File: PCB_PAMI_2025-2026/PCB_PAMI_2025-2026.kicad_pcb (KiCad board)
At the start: 2 copper layers, 125 x 84 mm, 63 parts, among them J1 BAU, J10 MOTOR 4, J11 COMM_inter_mcu, J12 USB_C_Receptacle_USB2.0_16P, J13 BOOST_OUT, J2 BAT+, J3 VIN_Connector, J4 BAT-, J6 BOOST_IN, J7 MOTOR 3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

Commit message: corrections pins drivers trop proches
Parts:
- moved J9 1.62 mm to (131.3, 45.7)
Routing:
- net /3V3: track 152.4 -> 160.7 mm
- net /ENC2_2: track 66.5 -> 68.9 mm
- net /AOUT1: track 18.1 -> 19.8 mm
- net GND: track 108.5 -> 107.6 mm, vias 30 -> 28
- net /ENC1_1: track 54.8 -> 54.1 mm
- net /AOUT2: track 4.97 -> 5.64 mm
- net /ENC1_2: track 60.3 -> 59.6 mm
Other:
- outline, holes or cut-outs redrawn
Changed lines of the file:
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@@
 	(footprint "Connector_PinHeader_2.54mm:PinHeader_1x06_P2.54mm_Vertical"
 		(layer "F.Cu")
-		(at 131.34 44.1 90)
+		(at 131.34 45.72 90)
 		(descr "Through hole straight pin header, 1x06, 2.54mm pitch, single row")
 		(tags "Through hole pin header THT 1x06 2.54mm single row")
@@
 	)
 	(gr_rect
-		(start 94 35.9)
-		(end 98 43.9)
+		(start 87.44 36.64)
+		(end 97.98 40.64)
 		(stroke
 			(width 0.2)
@@
 	)
 	(gr_rect
-		(start 94 68)
-		(end 98 76)
+		(start 87.44 69.66)
+		(end 97.98 73.66)
 		(stroke
 			(width 0.2)
@@
 	)
 	(segment
+		(start 133.799 54.795423)
+		(end 137.494423 51.1)
+		(width 1.5)
+		(layer "F.Cu")
+		(net 2)
+	)
+	(segment
 		(start 132.3 55.5)
 		(end 132.2 55.4)
@@
 	)
 	(segment
+		(start 137.494423 51.1)
+		(end 138 51.1)
+		(width 1.5)
+		(layer "F.Cu")
+		(net 2)
+	)
+	(segment
 		(start 161.1 25.75)
 		(end 161.1 24.93)
@@
 	)
 	(segment
-		(start 137.16 60.96)
-		(end 137.16 58.24)
-		(width 1.5)
-		(layer "F.Cu")
-		(net 2)
-	)
-	(segment
 		(start 55.43 93.75)
 		(end 57.15 93.75)
@@
 	)
 	(segment
-		(start 133.799 54.795423)
-		(end 140.194423 48.4)
-		(width 1.5)
-		(layer "F.Cu")
-		(net 2)
-	)
-	(segment
 		(start 142.24 88.46)
 		(end 142.3 88.4)
@@
 	)
 	(segment
-		(start 140.194423 48.4)
-		(end 141.5 48.4)
-		(width 1.5)
-		(layer "F.Cu")
-		(net 2)
-	)
-	(segment
 		(start 161.524264 26.9)
 		(end 161.6 26.975736)
@@
 		(net 2)
 	)
-	(segment
-		(start 137.16 58.24)
-		(end 137.2 58.2)
-		(width 1.5)
-		(layer "F.Cu")
-		(net 2)
-	)
 	(via
 		(at 73.5 67.7)
@@
 	)
 	(via
-		(at 137.2 58.2)
-		(size 0.6)
-		(drill 0.3)
-		(layers "F.Cu" "B.Cu")
-		(net 2)
-	)
-	(via
 		(at 115 44.1)
 		(size 0.6)
@@
 	)
 	(via
-		(at 141.5 48.4)
-		(size 0.6)
-		(drill 0.3)
-		(layers "F.Cu" "B.Cu")
-		(net 2)
-	)
-	(via
 		(at 115 68.2)
 		(size 0.6)
@@
 	)
 	(segment
+		(start 138 51.1)
+		(end 144.2 51.1)
+		(width 1.5)
+		(layer "B.Cu")
+		(net 2)
+	)
+	(segment
 		(start 141.5 39.9)
 		(end 141.5 37.1)
@@
 	)
 	(segment
+		(start 144.2 51.1)
+		(end 144.4 51.3)
+		(width 1.5)
+		(layer "B.Cu")
+		(net 2)
+	)
+	(segment
 		(start 148.485 32.8)
 		(end 148.525 32.76)
@@
 	)
 	(segment
-		(start 169.825 28.725)
-		(end 169.9 28.8)
+		(start 133.88 45.72)
+		(end 133.88 39.9)
 		(width 1)
 		(layer "F.Cu")
@@
 	)
 	(segment
-		(start 133.88 44.1)
-		(end 133.88 39.9)
+		(start 169.825 28.725)
+		(end 169.9 28.8)
 		(width 1)
 		(layer "F.Cu")
@@
 	)
 	(segment
+		(start 133.88 40.462)
+		(end 133.88 39.9)
+		(width 1)
+		(layer "B.Cu")
+		(net 7)
+	)
+	(segment
 		(start 126.3 41.838)
 		(end 139.338 28.8)
@@
 	)
 	(segment
-		(start 126.3 45.651)
-		(end 126.3 41.838)
+		(start 133.88 44.517919)
+		(end 133.88 45.72)
 		(width 1)
 		(layer "B.Cu")
@@
 	)
 	(segment
-		(start 132.649 45.651)
-		(end 133.88 44.42)
+		(start 133.083081 43.721)
+		(end 133.88 44.517919)
+		(width 1)
+		(layer "B.Cu")
+		(net 7)
+	)
+	(segment
+		(start 126.3 45.651)
+		(end 126.3 41.838)
 		(width 1)
 		(layer "B.Cu")
@@
 	)
 	(segment
+		(start 130.621 43.721)
+		(end 133.88 40.462)
+		(width 1)
+		(layer "B.Cu")
+		(net 7)
+	)
+	(segment
 		(start 94.8 45.5)
 		(end 94.951 45.651)
@@
 	)
 	(segment
+		(start 130.621 43.721)
+		(end 133.083081 43.721)
+		(width 1)
+		(layer "B.Cu")
+		(net 7)
+	)
+	(segment
 		(start 126.3 45.651)
-		(end 132.649 45.651)
+		(end 128.691 45.651)
 		(width 1)
 		(layer "B.Cu")
@@
 	)
 	(segment
-		(start 133.88 44.42)
-		(end 133.88 44.1)
+		(start 128.691 45.651)
+		(end 130.621 43.721)
 		(width 1)
 		(layer "B.Cu")
@@
 	)
 	(segment
-		(start 138.768884 39.9)
-		(end 135.056 43.612884)
+		(start 138.96 39.9)
+		(end 138.768884 39.9)
 		(width 0.25)
 		(layer "B.Cu")
@@
 	)
 	(segment
-		(start 135.056 44.587116)
-		(end 133.166116 46.477)
+		(start 138.96 39.9)
+		(end 135.1 43.76)
 		(width 0.25)
 		(layer "B.Cu")
@@
 	)
 	(segment
-		(start 138.96 39.9)
-		(end 138.768884 39.9)
+		(start 133.3 48.045)
+		(end 96.17686 48.045)
 		(width 0.25)
 		(layer "B.Cu")
@@
 	)
 	(segment
-		(start 94.60886 46.477)
-		(end 94.37586 46.244)
+		(start 77.396 46.244)
+		(end 76.27 47.37)
 		(width 0.25)
 		(layer "B.Cu")
@@
 	)
 	(segment
-		(start 133.166116 46.477)
-		(end 94.60886 46.477)
+		(start 94.37586 46.244)
+		(end 77.396 46.244)
 		(width 0.25)
 		(layer "B.Cu")
@@
 	)
 	(segment
-		(start 94.37586 46.244)
-		(end 77.396 46.244)
+		(start 96.17686 48.045)
+		(end 94.37586 46.244)
 		(width 0.25)
 		(layer "B.Cu")
@@
 	)
 	(segment
-		(start 77.396 46.244)
-		(end 76.27 47.37)
+		(start 135.1 43.76)
+		(end 135.1 46.245)
 		(width 0.25)
 		(layer "B.Cu")
@@
 	)
 	(segment
-		(start 135.056 43.612884)
-		(end 135.056 44.587116)
+		(start 135.1 46.245)
+		(end 133.3 48.045)
 		(width 0.25)
 		(layer "B.Cu")
@@
 	)
 	(segment
-		(start 134.113 48.947)
-		(end 82.927 48.947)
+		(start 82.927 48.947)
+		(end 135.733 48.947)
 		(width 0.25)
 		(layer "B.Cu")
@@
 	)
 	(segment
-		(start 82.927 48.947)
-		(end 81.35 47.37)
+		(start 81.35 47.37)
+		(end 82.927 48.947)
 		(width 0.25)
 		(layer "B.Cu")
@@
 	)
 	(segment
-		(start 138.96 44.1)
-		(end 134.113 48.947)
+		(start 135.733 48.947)
+		(end 138.96 45.72)
 		(width 0.25)
 		(layer "B.Cu")
@@
 	(segment
 		(start 148.525 45.46)
-		(end 148.084 45.901)
+		(end 147.84 45.46)
+		(width 1.5)
+		(layer "F.Cu")
+		(net 27)
+	)
+	(segment
+		(start 145 48.3)
+		(end 133.3 48.3)
 		(width 1.5)
 		(layer "F.Cu")
@@
 	)
 	(segment
-		(start 133.134001 45.901)
-		(end 131.34 44.106999)
+		(start 147.84 45.46)
+		(end 145 48.3)
 		(width 1.5)
 		(layer "F.Cu")
@@
 	)
 	(segment
-		(start 131.34 44.106999)
-		(end 131.34 44.1)
+		(start 131.34 46.34)
+		(end 131.34 45.72)
 		(width 1.5)
 		(layer "F.Cu")
@@
 	)
 	(segment
-		(start 148.084 45.901)
-		(end 133.134001 45.901)
+		(start 133.3 48.3)
+		(end 131.34 46.34)
 		(width 1.5)
 		(layer "F.Cu")
@@
 	)
 	(segment
-		(start 132.024 48.496)
+		(start 83.89 47.37)
 		(end 85.016 48.496)
 		(width 0.25)
@@
 	)
 	(segment
-		(start 85.016 48.496)
-		(end 83.89 47.37)
+		(start 133.644 48.496)
+		(end 136.42 45.72)
 		(width 0.25)
 		(layer "B.Cu")
@@
 	)
 	(segment
-		(start 136.42 44.1)
-		(end 132.024 48.496)
+		(start 85.016 48.496)
+		(end 133.644 48.496)
 		(width 0.25)
 		(layer "B.Cu")
@@
 	)
 	(segment
-		(start 145.22 42.92)
-		(end 144.04 44.1)
+		(start 146.84 42.92)
+		(end 144.04 45.72)
 		(width 1.5)
 		(layer "F.Cu")
@@
 	(segment
 		(start 148.525 42.92)
-		(end 145.22 42.92)
+		(end 146.84 42.92)
 		(width 1.5)
 		(layer "F.Cu")
@@
 	(segment
 		(start 158.685 45.46)
-		(end 144.361 59.784)
+		(end 145.545 58.6)
 		(width 0.25)
 		(layer "B.Cu")
@@
 	)
 	(segment
-		(start 144.361 59.784)
-		(end 79.096 59.784)
+		(start 80.28 58.6)
+		(end 76.27 62.61)
 		(width 0.25)
 		(layer "B.Cu")
@@
 	)
 	(segment
-		(start 79.096 59.784)
-		(end 76.27 62.61)
+		(start 145.545 58.6)
+		(end 80.28 58.6)
 		(width 0.25)
 		(layer "B.Cu")

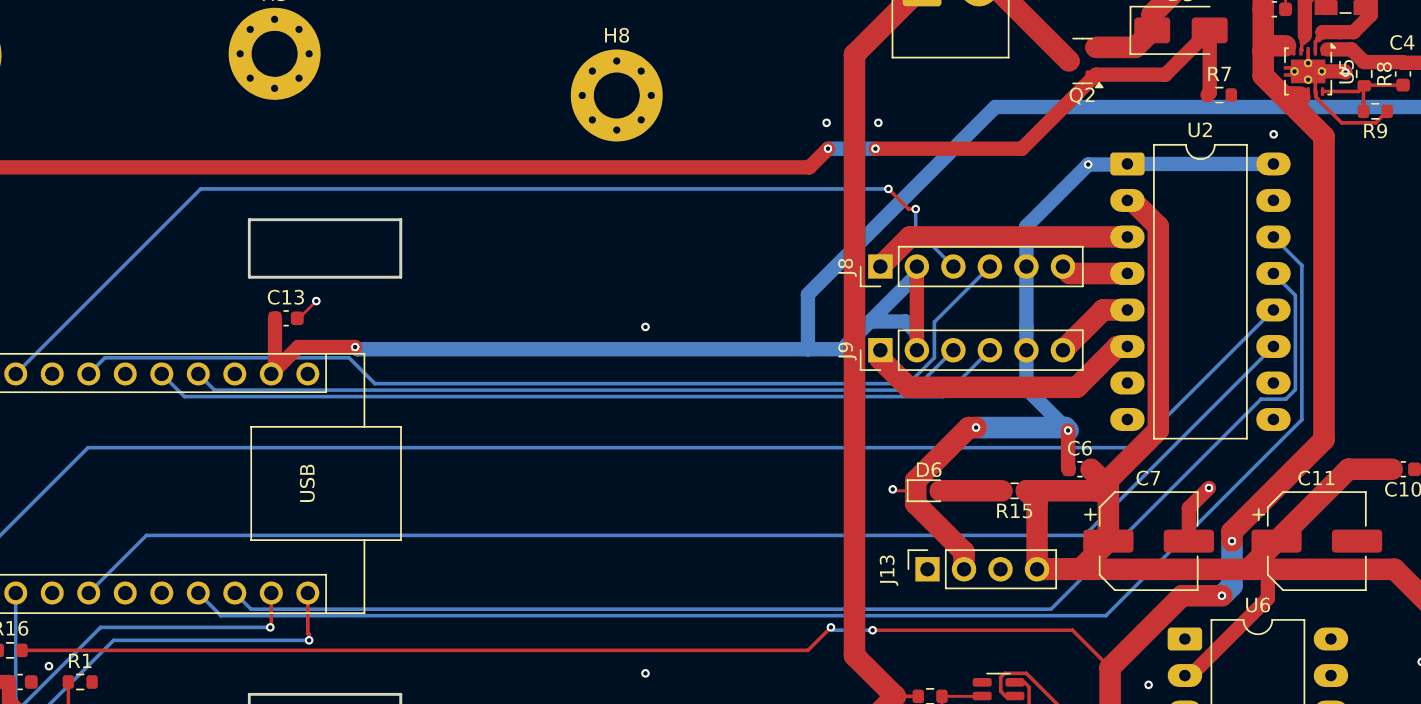
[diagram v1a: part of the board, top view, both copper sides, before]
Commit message: ajustement de l'emplacement de certaines pièces
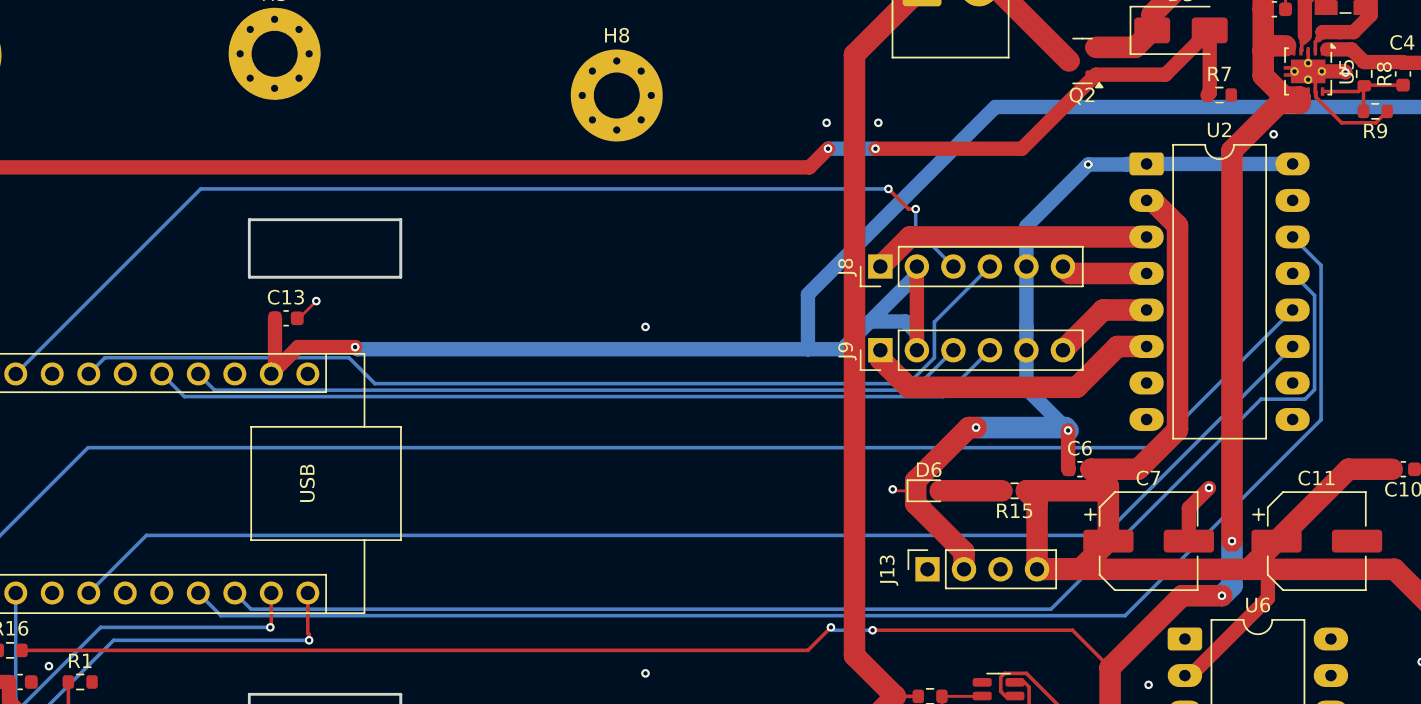
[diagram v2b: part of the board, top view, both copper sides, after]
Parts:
- moved U2 1.34 mm to (149.9, 32.8)
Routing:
- net GND: track 107.6 -> 108.9 mm
- net /BOUT2: track 4.68 -> 6.02 mm
- net /BOUT1: track 18.0 -> 19.4 mm
- net /BIN2: track 100.7 -> 102.1 mm
- net /BIN1: track 89.5 -> 90.9 mm
- net /AOUT2: track 5.64 -> 6.98 mm
- net /AOUT1: track 19.8 -> 21.1 mm
- net /AIN1: track 96.6 -> 97.9 mm
- net /AIN2: track 89.3 -> 90.6 mm
- net /6V: track 98.3 -> 99.5 mm
- net /REG_IN: track 176.3 -> 175.3 mm
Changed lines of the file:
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@@
 	(footprint "Package_DIP:DIP-16_W10.16mm_LongPads"
 		(layer "F.Cu")
-		(at 148.525 32.76)
+		(at 149.86 32.76)
 		(descr "16-lead though-hole mounted DIP package, row spacing 10.16mm (400 mils), LongPads")
 		(tags "THT DIP DIL PDIP 2.54mm 10.16mm 400mil LongPads")
@@
 	)
 	(segment
-		(start 138 51.1)
-		(end 144.2 51.1)
-		(width 1.5)
+		(start 148.525 32.76)
+		(end 160.02 32.76)
+		(width 1)
 		(layer "B.Cu")
 		(net 2)
 	)
 	(segment
-		(start 141.5 39.9)
-		(end 141.5 37.1)
-		(width 1)
+		(start 138 51.1)
+		(end 144.2 51.1)
+		(width 1.5)
 		(layer "B.Cu")
 		(net 2)
 	)
 	(segment
-		(start 141.5 44.1)
-		(end 141.5 39.9)
+		(start 145.8 32.8)
+		(end 148.485 32.8)
 		(width 1)
 		(layer "B.Cu")
@@
 	)
 	(segment
-		(start 145.8 32.8)
-		(end 148.485 32.8)
+		(start 141.5 39.9)
+		(end 141.5 37.1)
 		(width 1)
 		(layer "B.Cu")
@@
 	)
 	(segment
-		(start 148.525 32.76)
-		(end 158.685 32.76)
+		(start 141.5 44.1)
+		(end 141.5 39.9)
 		(width 1)
 		(layer "B.Cu")
@@
 	)
 	(segment
-		(start 148.485 32.8)
-		(end 148.525 32.76)
+		(start 141.5 48.4)
+		(end 144.4 51.3)
 		(width 1)
 		(layer "B.Cu")
@@
 	)
 	(segment
-		(start 141.5 48.4)
-		(end 144.4 51.3)
+		(start 148.485 32.8)
+		(end 148.525 32.76)
 		(width 1)
 		(layer "B.Cu")
@@
 	)
 	(segment
-		(start 158.9 59)
-		(end 163.9 54)
+		(start 149.86 35.3)
+		(end 150.26 35.3)
 		(width 1.5)
 		(layer "F.Cu")
@@
 	)
 	(segment
-		(start 147.2 55.2)
-		(end 146 54)
+		(start 158.9 59)
+		(end 163.9 54)
 		(width 1.5)
 		(layer "F.Cu")
@@
 	)
 	(segment
-		(start 146.441288 55.5)
-		(end 150.676 51.265288)
+		(start 147.2 55.2)
+		(end 146 54)
 		(width 1.5)
 		(layer "F.Cu")
@@
 	)
 	(segment
-		(start 148.861288 35.3)
-		(end 148.525 35.3)
-		(width 1.5)
-		(layer "F.Cu")
-		(net 8)
-	)
-	(segment
-		(start 150.676 51.265288)
-		(end 150.676 37.114712)
-		(width 1.5)
-		(layer "F.Cu")
-		(net 8)
-	)
-	(segment
 		(start 163.9 54)
 		(end 166.95 54)
@@
 	)
 	(segment
+		(start 149.276288 54)
+		(end 146 54)
+		(width 1.5)
+		(layer "F.Cu")
+		(net 8)
+	)
+	(segment
 		(start 147.2 59)
 		(end 147.2 55.2)
@@
 	)
 	(segment
-		(start 150.676 37.114712)
-		(end 148.861288 35.3)
+		(start 150.26 35.3)
+		(end 152.011 37.051)
 		(width 1.5)
 		(layer "F.Cu")
@@
 	)
 	(segment
+		(start 152.011 51.265288)
+		(end 149.276288 54)
+		(width 1.5)
+		(layer "F.Cu")
+		(net 8)
+	)
+	(segment
 		(start 170.993001 64.84)
 		(end 171 64.84)
@@
 	)
 	(segment
+		(start 152.011 37.051)
+		(end 152.011 51.265288)
+		(width 1.5)
+		(layer "F.Cu")
+		(net 8)
+	)
+	(segment
 		(start 156.94 60.96)
 		(end 158.3 60.96)
@@
 	)
 	(segment
+		(start 160.529 28.523242)
+		(end 159.107576 28.523242)
+		(width 1.5)
+		(layer "F.Cu")
+		(net 9)
+	)
+	(segment
 		(start 157.975 24.9)
 		(end 158.331 24.544)
@@
 	)
 	(segment
-		(start 162.2 30.85199)
-		(end 162.2 51.944602)
-		(width 1.5)
-		(layer "F.Cu")
-		(net 9)
-	)
-	(segment
 		(start 130.8 65.2)
 		(end 144.710398 65.2)
@@
 	)
 	(segment
-		(start 159.45401 28.106)
-		(end 162.2 30.85199)
+		(start 159.107576 28.523242)
+		(end 155.8 31.830818)
 		(width 1.5)
 		(layer "F.Cu")
@@
 	)
 	(segment
-		(start 159.45401 28.106)
-		(end 157.975 26.62699)
+		(start 155.8 31.830818)
+		(end 155.8 59)
 		(width 1.5)
 		(layer "F.Cu")
@@
 	)
 	(segment
-		(start 155.1 62.8)
-		(end 152.329602 62.8)
+		(start 160.529 28.523242)
+		(end 160.529 28.106)
 		(width 1.5)
 		(layer "F.Cu")
@@
 	)
 	(segment
-		(start 162.2 51.944602)
-		(end 155.8 58.344602)
+		(start 159.45401 28.106)
+		(end 157.975 26.62699)
+		(width 1.5)
+		(layer "F.Cu")
+		(net 9)
+	)
+	(segment
+		(start 155.1 62.8)
+		(end 152.329602 62.8)
 		(width 1.5)
 		(layer "F.Cu")
@@
 	)
 	(segment
-		(start 155.8 58.344602)
-		(end 155.8 59)
-		(width 1.5)
-		(layer "F.Cu")
-		(net 9)
-	)
-	(segment
 		(start 147.32 91.465)
 		(end 147.32 67.809602)
@@
 	)
 	(segment
-		(start 148.525 37.84)
-		(end 133.393001 37.84)
+		(start 131.34 39.893001)
+		(end 131.34 39.9)
 		(width 1.5)
 		(layer "F.Cu")
@@
 	)
 	(segment
-		(start 131.34 39.893001)
-		(end 131.34 39.9)
+		(start 149.86 37.84)
+		(end 133.393001 37.84)
 		(width 1.5)
 		(layer "F.Cu")
@@
 	)
 	(segment
-		(start 148.525 40.38)
+		(start 149.86 40.38)
 		(end 144.52 40.38)
 		(width 1.5)
@@
 	)
 	(segment
-		(start 148.525 45.46)
-		(end 147.84 45.46)
+		(start 147.84 45.46)
+		(end 145 48.3)
 		(width 1.5)
 		(layer "F.Cu")
@@
 	)
 	(segment
-		(start 145 48.3)
-		(end 133.3 48.3)
+		(start 131.34 46.34)
+		(end 131.34 45.72)
 		(width 1.5)
 		(layer "F.Cu")
@@
 	)
 	(segment
-		(start 147.84 45.46)
-		(end 145 48.3)
+		(start 145 48.3)
+		(end 133.3 48.3)
 		(width 1.5)
 		(layer "F.Cu")
@@
 	)
 	(segment
-		(start 131.34 46.34)
-		(end 131.34 45.72)
+		(start 133.3 48.3)
+		(end 131.34 46.34)
 		(width 1.5)
 		(layer "F.Cu")
@@
 	)
 	(segment
-		(start 133.3 48.3)
-		(end 131.34 46.34)
+		(start 149.86 45.46)
+		(end 147.84 45.46)
 		(width 1.5)
 		(layer "F.Cu")
@@
 	)
 	(segment
-		(start 146.84 42.92)
-		(end 144.04 45.72)
+		(start 149.86 42.92)
+		(end 146.84 42.92)
 		(width 1.5)
 		(layer "F.Cu")
@@
 	)
 	(segment
-		(start 148.525 42.92)
-		(end 146.84 42.92)
+		(start 146.84 42.92)
+		(end 144.04 45.72)
 		(width 1.5)
 		(layer "F.Cu")
@@
 	)
 	(segment
-		(start 157.818596 49.126)
-		(end 143.208596 63.736)
+		(start 161.546 41.906)
+		(end 161.546 48.466404)
 		(width 0.25)
 		(layer "B.Cu")
@@
 	)
 	(segment
-		(start 160.211 48.466404)
-		(end 159.551404 49.126)
+		(start 161.546 48.466404)
+		(end 160.886404 49.126)
 		(width 0.25)
 		(layer "B.Cu")
@@
 	)
 	(segment
-		(start 158.685 40.38)
-		(end 160.211 41.906)
+		(start 157.818596 49.126)
+		(end 143.208596 63.736)
 		(width 0.25)
 		(layer "B.Cu")
@@
 	)
 	(segment
-		(start 159.551404 49.126)
+		(start 160.886404 49.126)
 		(end 157.818596 49.126)
 		(width 0.25)
@@
 	)
 	(segment
-		(start 160.211 41.906)
-		(end 160.211 48.466404)
+		(start 160.02 40.38)
+		(end 161.546 41.906)
 		(width 0.25)
 		(layer "B.Cu")
@@
 	)
 	(segment
-		(start 160.662 39.817)
-		(end 160.662 50.555404)
+		(start 148.365404 64.187)
+		(end 85.467 64.187)
 		(width 0.25)
 		(layer "B.Cu")
@@
 	)
 	(segment
-		(start 85.467 64.187)
-		(end 83.89 62.61)
+		(start 160.02 37.84)
+		(end 161.997 39.817)
 		(width 0.25)
 		(layer "B.Cu")
@@
 	)
 	(segment
-		(start 147.030404 64.187)
-		(end 85.467 64.187)
+		(start 161.997 50.555404)
+		(end 148.365404 64.187)
 		(width 0.25)
 		(layer "B.Cu")
@@
 	)
 	(segment
-		(start 158.685 37.84)
-		(end 160.662 39.817)
+		(start 85.467 64.187)
+		(end 83.89 62.61)
 		(width 0.25)
 		(layer "B.Cu")
@@
 	)
 	(segment
-		(start 160.662 50.555404)
-		(end 147.030404 64.187)
+		(start 161.997 39.817)
+		(end 161.997 50.555404)
 		(width 0.25)
 		(layer "B.Cu")
@@
 	)
 	(segment
-		(start 158.685 45.46)
-		(end 145.545 58.6)
+		(start 160.02 45.46)
+		(end 146.88 58.6)
 		(width 0.25)
 		(layer "B.Cu")
@@
 	)
 	(segment
-		(start 145.545 58.6)
+		(start 146.88 58.6)
 		(end 80.28 58.6)
 		(width 0.25)
@@
 	)
 	(segment
-		(start 158.685 42.92)
-		(end 149.105 52.5)
+		(start 150.44 52.5)
+		(end 76.22 52.5)
 		(width 0.25)
 		(layer "B.Cu")
@@
 	)
 	(segment
-		(start 76.22 52.5)
-		(end 66.11 62.61)
+		(start 160.02 42.92)
+		(end 150.44 52.5)
 		(width 0.25)
 		(layer "B.Cu")
@@
 	)
 	(segment
-		(start 149.105 52.5)
-		(end 76.22 52.5)
+		(start 76.22 52.5)
+		(end 66.11 62.61)
 		(width 0.25)
 		(layer "B.Cu")
